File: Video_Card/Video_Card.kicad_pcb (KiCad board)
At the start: 4 copper layers, 159.8 x 100 mm, 9 parts, among them J1 DIN41612_03x32_ABC_COMETbus, U1 74FCT16245, U2 74FCT162244, U3 74FCT162244

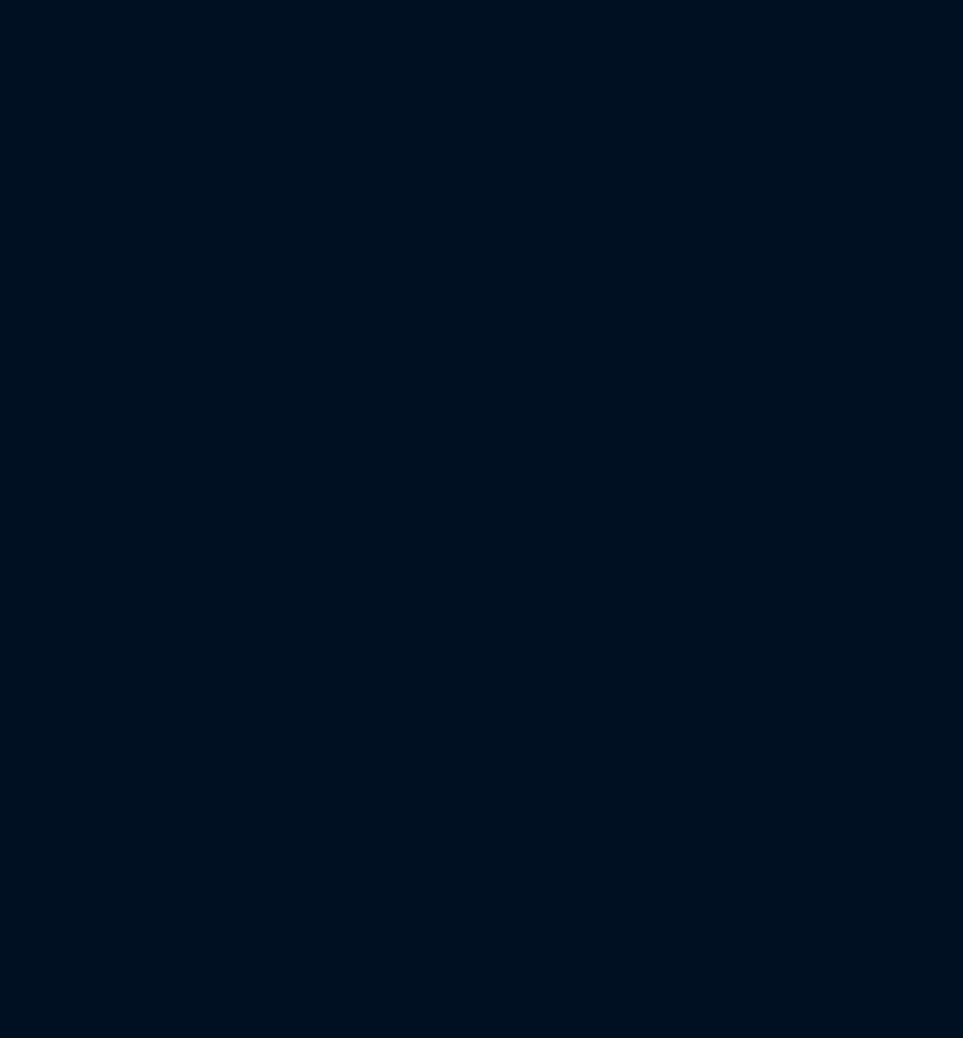
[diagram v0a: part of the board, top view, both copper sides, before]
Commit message: Todays work:
* Added clock identifier to SPI flash clock input
* Add config pins to FPGA host interface - can be used for configuring address decoding
* Add FPGA clocks sheet
* Add expansion ROM sheet
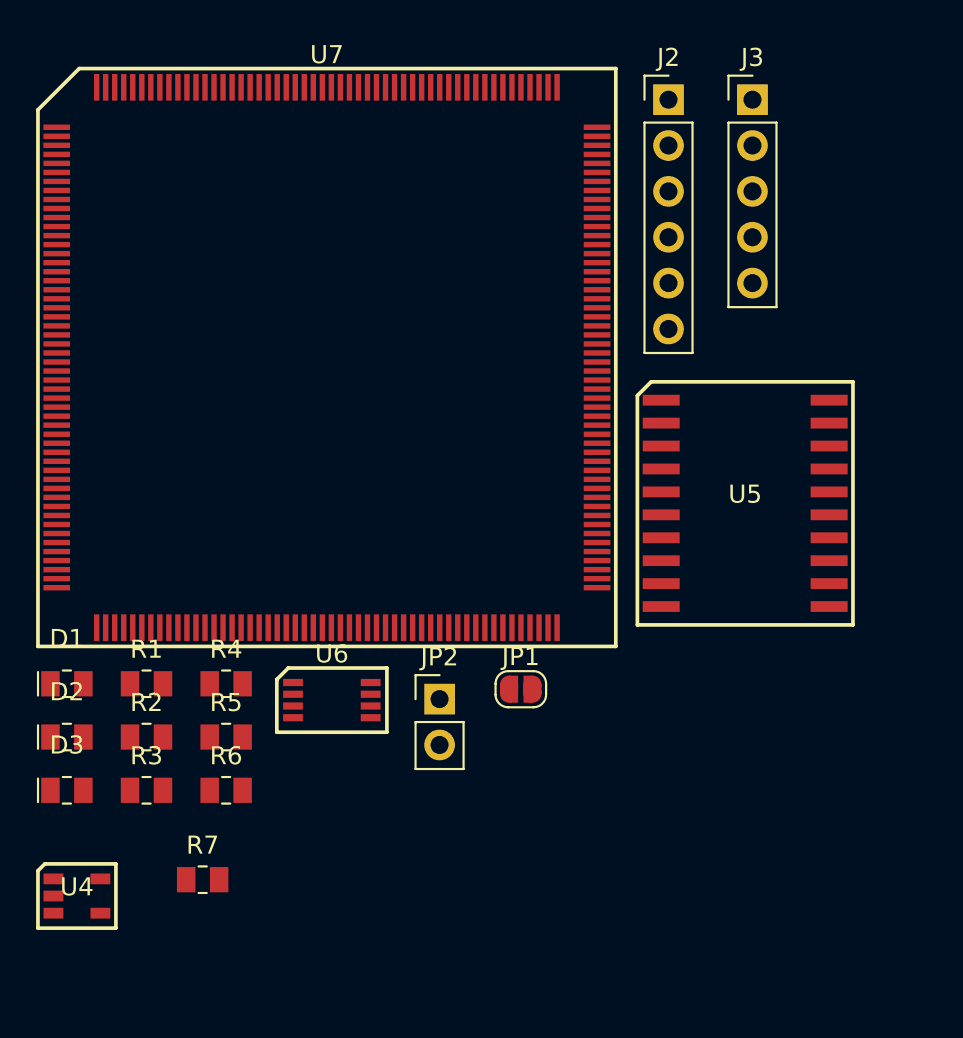
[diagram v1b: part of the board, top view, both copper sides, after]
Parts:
- added D1: GREEN, COMET_footprints:LED_SMD0805, F.Cu at (53.4, -24.1)
- added D2: GREEN, COMET_footprints:LED_SMD0805, F.Cu at (53.4, -21.2)
- added D3: RED, COMET_footprints:LED_SMD0805, F.Cu at (53.4, -18.2)
- added J2: Conn_01x06_Pin, Connector_PinHeader_2.54mm:PinHeader_1x06_P2.54mm_Vertical, F.Cu at (86.7, -56.5)
- added J3: Conn_01x05_Socket, Connector_PinHeader_2.54mm:PinHeader_1x05_P2.54mm_Vertical, F.Cu at (91.4, -56.5)
- added JP1: SolderJumper_2_Open, Jumper:SolderJumper-2_P1.3mm_Open_RoundedPad1.0x1.5mm, F.Cu at (78.5, -23.8)
- added JP2: Jumper_2_Open, Connector_PinHeader_2.54mm:PinHeader_1x02_P2.54mm_Vertical, F.Cu at (74.0, -23.3)
- added R1: 10K, COMET_footprints:R_SMD0805, F.Cu at (57.8, -24.1)
- added R2: 1K, COMET_footprints:R_SMD0805, F.Cu at (57.8, -21.2)
- added R3: 1K, COMET_footprints:R_SMD0805, F.Cu at (57.8, -18.2)
- added R4: 1K, COMET_footprints:R_SMD0805, F.Cu at (62.2, -24.1)
- added R5: 1K, COMET_footprints:R_SMD0805, F.Cu at (62.2, -21.2)
- added R6: 1K, COMET_footprints:R_SMD0805, F.Cu at (62.2, -18.2)
- added R7: 10K, COMET_footprints:R_SMD0805, F.Cu at (60.9, -13.3)
- added U4: SN74AHCT1G32DBV, COMET_footprints:Package_SOT23-5, F.Cu at (53.9, -12.4)
- added U5: PIC18F15Q40, COMET_footprints:Package_SO20W, F.Cu at (91.0, -34.1)
- added U6: ~, COMET_footprints:Package_TSSOP-8_3x3mm_P0.65mm, F.Cu at (68.1, -23.2)
- added U7: EPF81188AQC208-3, COMET_footprints:Package_PQFP-208_28x28mm_P0.5mm, F.Cu at (67.8, -42.2)
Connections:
- J1 pad b10: Net-(J1-Padb10) -> ~{AEIN}
- J1 pad b11: Net-(J1-Padb10) -> ~{AEOUT}
- J1 pad b15: unconnected-(J1-Padb15) -> CONFDONE
- U1 pad 10: unconnected-(U1C-GND-Pad10) -> GND
- U1 pad 15: unconnected-(U1C-GND-Pad15) -> GND
- U1 pad 18: unconnected-(U1C-VCC-Pad18) -> +5V
- U1 pad 21: unconnected-(U1C-GND-Pad21) -> GND
- U1 pad 28: unconnected-(U1C-GND-Pad28) -> GND
- U1 pad 31: unconnected-(U1C-VCC-Pad31) -> +5V
- U1 pad 34: unconnected-(U1C-GND-Pad34) -> GND
- U1 pad 39: unconnected-(U1C-GND-Pad39) -> GND
- U1 pad 4: unconnected-(U1C-GND-Pad4) -> GND
- U1 pad 42: unconnected-(U1C-VCC-Pad42) -> +5V
- U1 pad 45: unconnected-(U1C-GND-Pad45) -> GND
- U1 pad 7: unconnected-(U1C-VCC-Pad7) -> +5V
- U2 pad 10: unconnected-(U2E-GND-Pad10) -> GND
- U2 pad 11: unconnected-(U2B-2Y3-Pad11) -> A9
- U2 pad 12: unconnected-(U2B-2Y4-Pad12) -> A8
- U2 pad 13: unconnected-(U2C-3Y1-Pad13) -> A7
- U2 pad 14: unconnected-(U2C-3Y2-Pad14) -> A6
- U2 pad 15: unconnected-(U2E-GND-Pad15) -> GND
- U2 pad 16: unconnected-(U2C-3Y3-Pad16) -> A5
- U2 pad 17: unconnected-(U2C-3Y4-Pad17) -> A4
- U2 pad 18: unconnected-(U2E-VCC-Pad18) -> +5V
- U2 pad 19: unconnected-(U2D-4Y1-Pad19) -> A3
- U2 pad 2: unconnected-(U2A-1Y1-Pad2) -> A15
- U2 pad 20: unconnected-(U2D-4Y2-Pad20) -> A2
- U2 pad 21: unconnected-(U2E-GND-Pad21) -> GND
- U2 pad 22: unconnected-(U2D-4Y3-Pad22) -> A1
- U2 pad 26: unconnected-(U2D-4A4-Pad26) -> GND
- U2 pad 27: unconnected-(U2D-4A3-Pad27) -> SA1
- U2 pad 28: unconnected-(U2E-GND-Pad28) -> GND
- U2 pad 29: unconnected-(U2D-4A2-Pad29) -> SA2
- U2 pad 3: unconnected-(U2A-1Y2-Pad3) -> A14
- U2 pad 30: unconnected-(U2D-4A1-Pad30) -> SA3
- U2 pad 31: unconnected-(U2E-VCC-Pad31) -> +5V
- U2 pad 32: unconnected-(U2C-3A4-Pad32) -> SA4
- U2 pad 33: unconnected-(U2C-3A3-Pad33) -> SA5
- U2 pad 34: unconnected-(U2E-GND-Pad34) -> GND
- U2 pad 35: unconnected-(U2C-3A2-Pad35) -> SA6
- U2 pad 36: unconnected-(U2C-3A1-Pad36) -> SA7
- U2 pad 37: unconnected-(U2B-2A4-Pad37) -> SA8
- U2 pad 38: unconnected-(U2B-2A3-Pad38) -> SA9
- U2 pad 39: unconnected-(U2E-GND-Pad39) -> GND
- U2 pad 4: unconnected-(U2E-GND-Pad4) -> GND
- U2 pad 40: unconnected-(U2B-2A2-Pad40) -> SA10
- U2 pad 41: unconnected-(U2B-2A1-Pad41) -> SA11
- U2 pad 42: unconnected-(U2E-VCC-Pad42) -> +5V
- U2 pad 43: unconnected-(U2A-1A4-Pad43) -> SA12
- U2 pad 44: unconnected-(U2A-1A3-Pad44) -> SA13
- U2 pad 45: unconnected-(U2E-GND-Pad45) -> GND
- U2 pad 46: unconnected-(U2A-1A2-Pad46) -> SA14
- U2 pad 47: unconnected-(U2A-1A1-Pad47) -> SA15
- U2 pad 5: unconnected-(U2A-1Y3-Pad5) -> A13
- U2 pad 6: unconnected-(U2A-1Y4-Pad6) -> A12
- U2 pad 7: unconnected-(U2E-VCC-Pad7) -> +5V
- U2 pad 8: unconnected-(U2B-2Y1-Pad8) -> A11
- U2 pad 9: unconnected-(U2B-2Y2-Pad9) -> A10
- U3 pad 10: unconnected-(U3E-GND-Pad10) -> GND
- U3 pad 11: unconnected-(U3B-2Y3-Pad11) -> FC2
- U3 pad 12: unconnected-(U3B-2Y4-Pad12) -> ~{AS}
- U3 pad 13: unconnected-(U3C-3Y1-Pad13) -> A23
- U3 pad 14: unconnected-(U3C-3Y2-Pad14) -> A22
- U3 pad 15: unconnected-(U3E-GND-Pad15) -> GND
- U3 pad 16: unconnected-(U3C-3Y3-Pad16) -> A21
- U3 pad 17: unconnected-(U3C-3Y4-Pad17) -> A20
- U3 pad 18: unconnected-(U3E-VCC-Pad18) -> +5V
- U3 pad 19: unconnected-(U3D-4Y1-Pad19) -> A19
- U3 pad 2: unconnected-(U3A-1Y1-Pad2) -> ~{SYSRESET}
- U3 pad 20: unconnected-(U3D-4Y2-Pad20) -> A18
- U3 pad 21: unconnected-(U3E-GND-Pad21) -> GND
- U3 pad 22: unconnected-(U3D-4Y3-Pad22) -> A17
- U3 pad 23: unconnected-(U3D-4Y4-Pad23) -> A16
- U3 pad 26: unconnected-(U3D-4A4-Pad26) -> SA16
- U3 pad 27: unconnected-(U3D-4A3-Pad27) -> SA17
- U3 pad 28: unconnected-(U3E-GND-Pad28) -> GND
- U3 pad 29: unconnected-(U3D-4A2-Pad29) -> SA18
- U3 pad 3: unconnected-(U3A-1Y2-Pad3) -> ~{UDS}
- U3 pad 30: unconnected-(U3D-4A1-Pad30) -> SA19
- U3 pad 31: unconnected-(U3E-VCC-Pad31) -> +5V
- U3 pad 32: unconnected-(U3C-3A4-Pad32) -> SA20
- U3 pad 33: unconnected-(U3C-3A3-Pad33) -> SA21
- U3 pad 34: unconnected-(U3E-GND-Pad34) -> GND
- U3 pad 35: unconnected-(U3C-3A2-Pad35) -> SA22
- U3 pad 36: unconnected-(U3C-3A1-Pad36) -> SA23
- U3 pad 37: unconnected-(U3B-2A4-Pad37) -> ~{AS`}
- U3 pad 38: unconnected-(U3B-2A3-Pad38) -> FC2`
- U3 pad 39: unconnected-(U3E-GND-Pad39) -> GND
- U3 pad 4: unconnected-(U3E-GND-Pad4) -> GND
- U3 pad 40: unconnected-(U3B-2A2-Pad40) -> FC1`
- U3 pad 41: unconnected-(U3B-2A1-Pad41) -> FC0`
- U3 pad 42: unconnected-(U3E-VCC-Pad42) -> +5V
- U3 pad 43: unconnected-(U3A-1A4-Pad43) -> ~{WRITE`}
- U3 pad 44: unconnected-(U3A-1A3-Pad44) -> ~{LDS`}
- U3 pad 45: unconnected-(U3E-GND-Pad45) -> GND
- U3 pad 46: unconnected-(U3A-1A2-Pad46) -> ~{UDS`}
- U3 pad 47: unconnected-(U3A-1A1-Pad47) -> ~{SYSRESET`}
- U3 pad 5: unconnected-(U3A-1Y3-Pad5) -> ~{LDS}
- U3 pad 6: unconnected-(U3A-1Y4-Pad6) -> ~{WRITE}
- U3 pad 7: unconnected-(U3E-VCC-Pad7) -> +5V
- U3 pad 8: unconnected-(U3B-2Y1-Pad8) -> FC0
- U3 pad 9: unconnected-(U3B-2Y2-Pad9) -> FC1

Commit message: Work to date
So much to list ....

* Changed expansion ROM to 16 bit wide to remove some components
* Tried moving peripherals over to an 8 bit dedicated bus, but will have to revert this to reduce component count
* Fleshed out keyboard and I2C controller circuits
* Tried to fit in a font RAM, but I am 50/50 whether this will stick

And a lot more I am sure.
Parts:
- removed the D1 at (53.4, -24.1)
- added C1: 100nF, COMET_footprints:C_SMD0805, F.Cu at (87.1, 128.3)
- added C10: 100pF, COMET_footprints:C_SMD0805, F.Cu at (78.7, 127.3)
- added C2: 22uF, COMET_footprints:C_SMD_3.2MMx6.0MM, F.Cu at (85.6, 140.2)
- added C3: 100nF, COMET_footprints:C_SMD0805, F.Cu at (83.3, 134.6)
- added C4: 100nF, COMET_footprints:C_SMD0805, F.Cu at (99.8, 120.8)
- added C5: 47uF, COMET_footprints:C_SMD_3.2MMx6.0MM, F.Cu at (112.9, 138.8)
- added C6: 100nF, COMET_footprints:C_SMD0805, F.Cu at (5.44, 116.0)
- added C7: 100nF, COMET_footprints:C_SMD0805, F.Cu at (25.5, 133.9)
- added C8: 100nF, COMET_footprints:C_SMD0805, F.Cu at (77.7, 65.3)
- added C9: 100pF, COMET_footprints:C_SMD0805, F.Cu at (76.5, 127.3)
- added D4: 1N4148W, COMET_footprints:D_SOD-123, F.Cu at (99.7, 135.5)
- added D5: BAV99, COMET_footprints:Package_SOT-23, F.Cu at (82.7, 130.3)
- added D6: BAV99, COMET_footprints:Package_SOT-23, F.Cu at (83.5, 124.8)
- added D7: BAV99, COMET_footprints:Package_SOT-23, F.Cu at (87.2, 124.8)
- added D8: GREEN, COMET_footprints:LED_SMD0805, F.Cu at (128.8, 83.4)
- added F1: 2920L150DR, COMET_footprints:Fuse_2920_7451Metric, F.Cu at (76.5, 55.8)
- added HS1: ~, Video_Card:28MM-HEATSINK, F.Cu at (155.4, 79.6)
- added J4: DE15_Receptacle_HighDensity_MountingHoles, Video_Card:DSUB-15-HD_Female_Horizontal_P2.29x1.90mm_EdgePinOffset3.03mm_Housed_MountingHolesOffset4.94mm, F.Cu at (71.3, 124.2)
- added J5: Mini-DIN-6, Video_Card:Connector_MiniDIN-6, F.Cu at (64.0, 75.3)
- added J6: Mini-DIN-6, Video_Card:Connector_MiniDIN-6, F.Cu at (63.9, 92.8)
- added JP3: Jumper_2_Open, Connector_PinHeader_2.54mm:PinHeader_1x02_P2.54mm_Vertical, F.Cu at (36.4, 48.0)
- added JP4: Jumper_2_Open, Connector_PinHeader_2.54mm:PinHeader_1x02_P2.54mm_Vertical, F.Cu at (22.8, 65.5)
- added L1: ?, COMET_footprints:L_1812_4532Metric, F.Cu at (87.1, 133.1)
- added R10: 10K, COMET_footprints:R_SMD0805, F.Cu at (-3.38, 50.0)
- added R11: 10K, COMET_footprints:R_SMD0805, F.Cu at (31.9, 67.8)
- added R12: 0R, COMET_footprints:R_SMD0805, F.Cu at (-3.38, 53.0)
- added R13: 0R, COMET_footprints:R_SMD0805, F.Cu at (21.0, 84.4)
- added R14: 0R, COMET_footprints:R_SMD0805, F.Cu at (21.0, 87.3)
- added R15: 10K, COMET_footprints:R_SMD0805, F.Cu at (25.5, 136.8)
- added R16: 10K, COMET_footprints:R_SMD0805, F.Cu at (25.5, 139.8)
- added R17: 0R, COMET_footprints:R_SMD0805, F.Cu at (29.9, 133.9)
- added R18: 0R, COMET_footprints:R_SMD0805, F.Cu at (29.9, 136.8)
- added R19: 1K5, COMET_footprints:R_SMD0805, F.Cu at (-3.38, 55.9)
- added R20: 15R, COMET_footprints:R_MiniMELF_MMA-0204, F.Cu at (101.0, 131.4)
- added R21: 150R, COMET_footprints:R_MiniMELF_MMA-0204, F.Cu at (98.2, 131.4)
- added R22: 75R, COMET_footprints:R_MiniMELF_MMA-0204, F.Cu at (78.5, 141.7)
- added R23: 75R, COMET_footprints:R_MiniMELF_MMA-0204, F.Cu at (78.5, 138.9)
- added R24: 75R, COMET_footprints:R_MiniMELF_MMA-0204, F.Cu at (78.5, 136.1)
- added R25: 10K, COMET_footprints:R_SMD0805, F.Cu at (29.9, 139.8)
- added R26: 0R, COMET_footprints:R_SMD0805, F.Cu at (-16.0, 109.3)
- added R27: 10K, COMET_footprints:R_SMD0805, F.Cu at (-21.5, 134.3)
- added R28: 10K, COMET_footprints:R_SMD0805, F.Cu at (-21.5, 137.2)
- added R29: 10K, COMET_footprints:R_SMD0805, F.Cu at (5.44, 119.0)
- added R30: 10K, COMET_footprints:R_SMD0805, F.Cu at (5.44, 121.9)
- added R31: 1K5, COMET_footprints:R_SMD0805, F.Cu at (5.44, 124.9)
- added R32: 1K5, COMET_footprints:R_SMD0805, F.Cu at (5.44, 127.8)
- added R33: 1K5, COMET_footprints:R_SMD0805, F.Cu at (76.7, 122.3)
- added R34: 1K5, COMET_footprints:R_SMD0805, F.Cu at (79.7, 122.3)
- added R35: 1K5, COMET_footprints:R_SMD0805, F.Cu at (5.44, 136.7)
- added R36: 1K, COMET_footprints:R_SMD0805, F.Cu at (132.5, 83.4)
- added R37: 1K5, COMET_footprints:R_SMD0805, F.Cu at (34.4, 133.9)
- added R38: 0R, COMET_footprints:R_SMD0805, F.Cu at (34.4, 136.8)
- added R39: 0R, COMET_footprints:R_SMD0805, F.Cu at (34.4, 139.8)
- added R4: 1K, COMET_footprints:R_SMD0805, F.Cu at (67.7, 65.2)
- added R44: 10K, COMET_footprints:R_SMD0805, F.Cu at (112.3, 93.6)
- added R45: 10K, COMET_footprints:R_SMD0805, F.Cu at (112.3, 91.2)
- added R46: 1K5, COMET_footprints:R_SMD0805, F.Cu at (90.2, 70.4)
- added R47: 1K5, COMET_footprints:R_SMD0805, F.Cu at (92.7, 70.4)
- added R48: 1K5, COMET_footprints:R_SMD0805, F.Cu at (90.0, 95.6)
- added R49: 1K5, COMET_footprints:R_SMD0805, F.Cu at (92.6, 95.6)
- added R50: 470R, COMET_footprints:R_SMD0805, F.Cu at (73.4, 65.3)
- added R51: 33R, COMET_footprints:R_SMD0805, F.Cu at (76.5, 131.8)
- added R52: 33R, COMET_footprints:R_SMD0805, F.Cu at (78.7, 131.8)
- added R53: 10K, COMET_footprints:R_SMD0805, F.Cu at (25.5, 84.4)
- added R54: 10K, COMET_footprints:R_SMD0805, F.Cu at (25.5, 87.3)
- added R7: 1K, COMET_footprints:R_SMD0805, F.Cu at (31.9, 64.8)
- added R8: 10K, COMET_footprints:R_SMD0805, F.Cu at (-3.38, 44.1)
- added R9: 10K, COMET_footprints:R_SMD0805, F.Cu at (-3.38, 47.1)
- added RN2: 10K, Resistor_SMD:R_Cat16-4, F.Cu at (-28.3, 92.7)
- added RN3: 10K, Resistor_SMD:R_Cat16-4, F.Cu at (-24.4, 92.7)
- added RN4: 10K, Resistor_SMD:R_Cat16-4, F.Cu at (32.2, 99.8)
- added RN5: 10K, Resistor_SMD:R_Cat16-4, F.Cu at (36.1, 99.8)
- added RN6: 10K, Resistor_SMD:R_Cat16-4, F.Cu at (-17.4, 135.2)
- added SW1: SW_DIP_x06, Button_Switch_SMD:SW_DIP_SPSTx06_Slide_6.7x16.8mm_W8.61mm_P2.54mm_LowProfile, B.Cu at (132.8, 137.4)
- added TP1: TestPoint, TestPoint:TestPoint_Pad_D1.0mm, F.Cu at (21.8, 133.9)
- added TP2: TestPoint, TestPoint:TestPoint_Pad_D1.0mm, F.Cu at (21.8, 137.0)
- added TP3: TestPoint, TestPoint:TestPoint_Pad_D1.0mm, F.Cu at (21.8, 140.0)
- added U10: SN74AHCT1G125DBV, COMET_footprints:Package_SOT23-5, F.Cu at (-2.82, 75.2)
- added U11: M29F400FB55N3F2, COMET_footprints:Package_TSOP-I-48_18.4x12mm_P0.5mm, F.Cu at (120.1, 119.1)
- added U14: IMSG171-35, COMET_footprints:Package_DIP-28_W15.24mm_LongPads, F.Cu at (99.8, 124.2)
- added U15: LM334M/NOPB, COMET_footprints:Package_SO8, F.Cu at (99.8, 114.8)
- added U16: SN74CBT16212CDLR, COMET_footprints:Package_SSOP56-1, F.Cu at (158.4, 110.7)
- added U17: SN74CBT16212CDLR, COMET_footprints:Package_SSOP56-1, F.Cu at (172.0, 110.8)
- added U18: SN74CBT16212CDLR, COMET_footprints:Package_SSOP56-1, F.Cu at (185.4, 110.6)
- added U19: IS61C6416AL-12TLI, COMET_footprints:Package_TSOP-II-44_10.16x18.41mm_P0.8mm, F.Cu at (158.2, 133.6)
- added U20: IS61C6416AL-12TLI, COMET_footprints:Package_TSOP-II-44_10.16x18.41mm_P0.8mm, F.Cu at (172.9, 133.6)
- added U21: SN74LVC1G19DBV, COMET_footprints:Package_SOT23-6, F.Cu at (-20.9, 110.2)
- added U22: IS61C6416AL-12TLI, COMET_footprints:Package_TSOP-II-44_10.16x18.41mm_P0.8mm, F.Cu at (187.6, 133.6)
- added U23: SST39SF010A-70-4C-NHE, COMET_footprints:Package_PLCC-32_SMD_socket, F.Cu at (138.9, 119.0)
- added U24: PCF8584T, COMET_footprints:Package_SO20W, F.Cu at (82.3, 112.0)
- added U25: VT82C42, COMET_footprints:Package_DIP-40_W15.24mm_LongPads, F.Cu at (91.4, 77.6)
- added U30: SN74AHCT1G32DBV, COMET_footprints:Package_SOT23-5, F.Cu at (23.7, 127.9)
- added U31: SN75452B, COMET_footprints:Package_DIP-8_W7.62mm_LongPads, F.Cu at (91.3, 62.5)
- added U32: SN75452B, COMET_footprints:Package_DIP-8_W7.62mm_LongPads, F.Cu at (91.4, 87.9)
- added U8: SN74LVC1G06DBV, COMET_footprints:Package_SOT23-5, F.Cu at (-2.82, 65.7)
- added U9: SN74LVC1G06DBV, COMET_footprints:Package_SOT23-5, F.Cu at (-2.82, 70.4)
- added Y1: 40MHz, COMET_footprints:Oscillator_SMD_XO91-4Pin_7.0x5.0mm, F.Cu at (182.6, 81.5)
- added Y2: 28.322MHz, COMET_footprints:Oscillator_DIP-8-14, F.Cu at (112.5, 58.5)
- added Y3: 25.175MHz, COMET_footprints:Oscillator_DIP-8-14, F.Cu at (112.8, 72.3)
- D1: value IN_USE -> GREEN
- R2, R3: value 1K -> 1K5
- U5: value PIC18F15Q40 -> PIC18F15Q40-I/SS; footprint COMET_footprints:Package_SO20W -> Video_Card:Package_SSOP-20_5.3x7.2mm_P0.65_MCHP
- U6: value ~ -> M95M04-DRDW6; footprint COMET_footprints:Package_TSSOP-8_3x3mm_P0.65mm -> COMET_footprints:Package_TSSOP-8_4.4x3mm_P0.65mm
- moved U7 150.1 mm to (155.4, 79.6), turned to 90 degrees
- moved D3 131.1 mm to (163.2, 53.3), turned to -90 degrees
- moved D2 130.8 mm to (160.9, 53.3), turned to -90 degrees
- moved R6 126.1 mm to (163.2, 57.3), turned to 90 degrees
- moved R5 126.1 mm to (160.9, 57.3), turned to 90 degrees
- moved J3 120.0 mm to (126.5, 58.3), turned to 90 degrees
- moved U6 118.6 mm to (156.8, 55.4), turned to 90 degrees
- moved J2 117.1 mm to (126.5, 53.7), turned to 90 degrees
- moved U5 106.4 mm to (148.5, 55.4), turned to 90 degrees
- moved JP1 38.2 mm to (71.9, 13.8)
- moved JP2 38.2 mm to (67.4, 14.4)
- moved R1 38.2 mm to (51.2, 13.5)
- moved R2 38.2 mm to (51.2, 16.5)
- moved R3 38.2 mm to (51.2, 19.4)
- moved R4 38.2 mm to (55.6, 13.5)
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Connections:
- D2 pad 1: Net-(D2-K) -> GND
- D3 pad 1: Net-(D3-K) -> GND
- J1 pad b10: ~{AEIN} -> Net-(J1B-~{AEIN})
- J1 pad b11: ~{AEOUT} -> Net-(J1B-~{AEIN})
- J1 pad b15: CONFDONE -> unconnected-(J1B-CONFDONE-Padb15)
- J3 pad 1: ~{SYSRESET} -> Net-(J3-Pin_1)
- R5 pad 1: Net-(D2-A) -> Net-(U5-LED_RUN)
- R5 pad 2: +5V -> Net-(D2-A)
- R6 pad 1: Net-(D3-A) -> Net-(U5-LED_FAIL)
- R6 pad 2: +5V -> Net-(D3-A)
- U5 pad 16: Net-(D3-K) -> Net-(U5-LED_FAIL)
- U5 pad 17: Net-(D2-K) -> Net-(U5-LED_RUN)
- U5 pad 4: ~{SYSRESET} -> Net-(J3-Pin_1)
- U5 pad 5: (no net) -> ~{FPGA_RESET}
- U7 pad 10: (no net) -> Net-(U14A-~{WR})
- U7 pad 100: (no net) -> A14
- U7 pad 101: (no net) -> A15
- U7 pad 112: (no net) -> DDIR
- U7 pad 116: (no net) -> SYSCLK
- U7 pad 117: (no net) -> D7
- U7 pad 118: (no net) -> D4
- U7 pad 120: (no net) -> D15
- U7 pad 121: (no net) -> D0
- U7 pad 125: (no net) -> A17
- U7 pad 126: (no net) -> Net-(RN2-R2.1)
- U7 pad 127: (no net) -> A19
- U7 pad 128: (no net) -> A20
- U7 pad 129: (no net) -> FC2
- U7 pad 13: (no net) -> ~{WRITE}
- U7 pad 130: (no net) -> FC0
- U7 pad 133: (no net) -> ~{UDS}
- U7 pad 134: (no net) -> A11
- U7 pad 135: (no net) -> ~{LDS}
- U7 pad 136: (no net) -> A2
- U7 pad 137: (no net) -> D13
- U7 pad 14: (no net) -> D3
- U7 pad 141: (no net) -> Net-(U14A-PCLK)
- U7 pad 142: (no net) -> D9
- U7 pad 144: (no net) -> D12
- U7 pad 145: (no net) -> D2
- U7 pad 146: (no net) -> ~{FPGA_RESET}
- U7 pad 149: (no net) -> Net-(U14A-P2)
- U7 pad 15: (no net) -> D1
- U7 pad 153: (no net) -> Net-(U14A-P3)
- U7 pad 160: (no net) -> A16
- U7 pad 162: (no net) -> A21
- U7 pad 163: (no net) -> A22
- U7 pad 164: (no net) -> A13
- U7 pad 167: (no net) -> Net-(U7F-VSYNC)
- U7 pad 169: (no net) -> Net-(U7F-CLK_25)
- U7 pad 17: (no net) -> D11
- U7 pad 170: (no net) -> Net-(U7F-HSYNC)
- U7 pad 173: (no net) -> Net-(U14A-P6)
- U7 pad 179: (no net) -> ~{DBEN}
- U7 pad 180: (no net) -> Net-(U7C-BERR_DRV)
- U7 pad 202: (no net) -> Net-(U7F-VID_ACT)
- U7 pad 22: (no net) -> A4
- U7 pad 23: (no net) -> A3
- U7 pad 24: (no net) -> D14
- U7 pad 25: (no net) -> D10
- U7 pad 26: (no net) -> A12
- U7 pad 29: (no net) -> FC1
- U7 pad 30: (no net) -> ~{AS}
- U7 pad 31: (no net) -> A18
- U7 pad 32: (no net) -> Net-(RN2-R1.1)
- U7 pad 37: (no net) -> D8
- U7 pad 38: (no net) -> D6
- U7 pad 39: (no net) -> D5
- U7 pad 40: (no net) -> Net-(U14A-P1)
- U7 pad 41: (no net) -> A1
- U7 pad 66: (no net) -> Net-(U14A-P0)
- U7 pad 7: (no net) -> Net-(U14A-P4)
- U7 pad 8: (no net) -> Net-(U14A-~{RD})
- U7 pad 83: (no net) -> Net-(U14A-~{BLANK})
- U7 pad 86: (no net) -> Net-(U14A-P7)
- U7 pad 90: (no net) -> Net-(U14A-P5)
- U7 pad 92: (no net) -> Net-(U7C-DTACK_DRV)
- U7 pad 95: (no net) -> Net-(U7F-CLK_28)
- U7 pad 99: (no net) -> A23
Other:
- board text added: "KEYBOARD"
- board text added: "MOUSE"
- board text added: "VGA COMPATIBLE VIDEO CARD TOM STOREY JUN 2025 REV ${REVISION}"
- board text removed: "VGA COMPATIBLE VIDEO CARD TOM STOREY MAR 2025 REV ${REVISION}"

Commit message: Final tweaks before ordering
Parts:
- removed JP4: Jumper_2_Open, Connector_PinHeader_2.54mm:PinHeader_1x02_P2.54mm_Vertical
- removed the R4 at (67.7, 65.2)
- removed the R4 at (55.6, 13.5)
- removed the R7 at (31.9, 64.8)
- removed the R7 at (54.3, 24.4)
- removed REF** (x2): MountingHole_3.2mm_M3, MountingHole:MountingHole_3.2mm_M3
- removed U30: SN74AHCT1G32DBV, COMET_footprints:Package_SOT23-5
- removed U31, U32: SN75452B, COMET_footprints:Package_DIP-8_W7.62mm_LongPads
- added C11: 47uF, COMET_footprints:C_SMD_3.2MMx6.0MM, F.Cu at (106.0, 85.1)
- added C12: 100nF, COMET_footprints:C_SMD0805, B.Cu at (206.1, 103.5)
- added C13: 100nF, COMET_footprints:C_SMD0805, B.Cu at (206.1, 94.6)
- added C14: 100nF, COMET_footprints:C_SMD0805, B.Cu at (201.6, 120.7)
- added C15: 100nF, COMET_footprints:C_SMD0805, B.Cu at (201.6, 129.5)
- added C16: 100nF, COMET_footprints:C_SMD0805, B.Cu at (206.1, 129.5)
- added C17: 100nF, COMET_footprints:C_SMD0805, B.Cu at (206.1, 120.7)
- added C18: 100nF, COMET_footprints:C_SMD0805, B.Cu at (204.2, 80.0)
- added C19: 100nF, COMET_footprints:C_SMD0805, B.Cu at (204.2, 85.3)
- added C20: 100nF, COMET_footprints:C_SMD0805, B.Cu at (162.9, 56.5)
- added C21: 100nF, COMET_footprints:C_SMD0805, B.Cu at (152.7, 56.6)
- added C22: 100nF, COMET_footprints:C_SMD0805, F.Cu at (136.8, 72.2)
- added C23: 100nF, COMET_footprints:C_SMD0805, F.Cu at (136.8, 80.2)
- added C24: 100nF, COMET_footprints:C_SMD0805, F.Cu at (136.8, 87.8)
- added C25: 100nF, COMET_footprints:C_SMD0805, F.Cu at (136.8, 92.8)
- added C26: 100nF, COMET_footprints:C_SMD0805, F.Cu at (150.0, 103.0)
- added C27: 100nF, COMET_footprints:C_SMD0805, F.Cu at (158.0, 103.0)
- added C28: 100nF, COMET_footprints:C_SMD0805, F.Cu at (170.0, 103.0)
- added C29: 100nF, COMET_footprints:C_SMD0805, F.Cu at (176.8, 93.8)
- added C30: 100nF, COMET_footprints:C_SMD0805, F.Cu at (176.8, 87.8)
- added C31: 100nF, COMET_footprints:C_SMD0805, F.Cu at (176.8, 79.8)
- added C32: 100nF, COMET_footprints:C_SMD0805, F.Cu at (176.8, 73.8)
- added C33: 100nF, COMET_footprints:C_SMD0805, B.Cu at (165.5, 63.0)
- added C34: 100nF, COMET_footprints:C_SMD0805, B.Cu at (155.5, 63.0)
- added C35: 100nF, COMET_footprints:C_SMD0805, B.Cu at (148.5, 63.0)
- added C36: 100nF, COMET_footprints:C_SMD0805, B.Cu at (144.0, 114.0)
- added C37: 100nF, COMET_footprints:C_SMD0805, B.Cu at (165.2, 116.0)
- added C38: 100nF, COMET_footprints:C_SMD0805, B.Cu at (184.9, 116.0)
- added C39: 100nF, COMET_footprints:C_SMD0805, B.Cu at (155.6, 135.0)
- added C40: 100nF, COMET_footprints:C_SMD0805, B.Cu at (155.6, 140.2)
- added C41: 100nF, COMET_footprints:C_SMD0805, B.Cu at (110.5, 58.4)
- added C42: 100nF, COMET_footprints:C_SMD0805, B.Cu at (110.5, 71.8)
- added C43: 100nF, COMET_footprints:C_SMD0805, B.Cu at (177.4, 135.0)
- added C44: 100nF, COMET_footprints:C_SMD0805, B.Cu at (177.4, 140.2)
- added C45: 100nF, COMET_footprints:C_SMD0805, B.Cu at (125.1, 112.4)
- added C46: 100nF, COMET_footprints:C_SMD0805, B.Cu at (125.1, 120.7)
- added C47: 100nF, COMET_footprints:C_SMD0805, B.Cu at (125.1, 128.9)
- added C48: 100nF, COMET_footprints:C_SMD0805, B.Cu at (116.8, 116.2)
- added C49: 100nF, COMET_footprints:C_SMD0805, B.Cu at (186.2, 79.5)
- added C50: 100nF, COMET_footprints:C_SMD0805, B.Cu at (83.6, 116.8)
- added C51: 100nF, COMET_footprints:C_SMD0805, B.Cu at (88.5, 101.6)
- added C52: 100nF, COMET_footprints:C_SMD0805, B.Cu at (92.7, 88.9)
- added C53: 100nF, COMET_footprints:C_SMD0805, B.Cu at (92.7, 71.1)
- added C54: 100nF, COMET_footprints:C_SMD0805, B.Cu at (185.8, 101.0)
- added C55: 100nF, COMET_footprints:C_SMD0805, B.Cu at (106.7, 133.3)
- added C56: 47uF, COMET_footprints:C_SMD_3.2MMx6.0MM, F.Cu at (88.3, 136.7)
- added C57: 100pF, COMET_footprints:C_SMD0805, F.Cu at (75.6, 125.1)
- added C58: 100pF, COMET_footprints:C_SMD0805, F.Cu at (75.6, 120.7)
- added C59: 100nF, COMET_footprints:C_SMD0805, F.Cu at (79.4, 139.1)
- added C60: 22uF, COMET_footprints:C_SMD_3.2MMx6.0MM, F.Cu at (88.3, 141.6)
- added C61: 100nF, COMET_footprints:C_SMD0805, B.Cu at (98.8, 141.0)
- added C62: 100nF, COMET_footprints:C_SMD0805, F.Cu at (77.5, 56.8)
- added H1: MountingHole_3.2mm_M3, MountingHole:MountingHole_3.2mm_M3, F.Cu at (67.0, 53.5)
- added H2: MountingHole_3.2mm_M3, MountingHole:MountingHole_3.2mm_M3, F.Cu at (67.0, 142.1)
- added R4: 1K5, COMET_footprints:R_SMD0805, F.Cu at (168.6, 60.3)
- added R40: 0R, COMET_footprints:R_SMD0805, B.Cu at (121.9, 58.4)
- added R41: 15R, COMET_footprints:R_SMD0805, F.Cu at (91.4, 122.6)
- added R42: 150R, COMET_footprints:R_SMD0805, F.Cu at (89.2, 129.2)
- added R43: 0R, COMET_footprints:R_SMD0805, B.Cu at (121.9, 71.8)
- added R55: 10K, COMET_footprints:R_SMD0805, F.Cu at (76.2, 107.3)
- added R56: 1K5, COMET_footprints:R_SMD0805, F.Cu at (81.0, 95.7)
- added R57: 1K5, COMET_footprints:R_SMD0805, F.Cu at (81.0, 93.7)
- added R58: 1K5, COMET_footprints:R_SMD0805, F.Cu at (81.0, 75.9)
- added R59: 1K5, COMET_footprints:R_SMD0805, F.Cu at (81.0, 74.0)
- added R60: 10K, COMET_footprints:R_SMD0805, F.Cu at (104.8, 94.0)
- added R61: 10K, COMET_footprints:R_SMD0805, F.Cu at (104.8, 91.4)
- added R62: 0R, COMET_footprints:R_SMD0805, F.Cu at (104.8, 96.5)
- added R63: 10K, COMET_footprints:R_SMD0805, F.Cu at (104.8, 101.4)
- added R64: 10K, COMET_footprints:R_SMD0805, F.Cu at (104.8, 99.1)
- added R65: 470R, COMET_footprints:R_SMD0805, F.Cu at (77.5, 58.5)
- added R66: 10K, COMET_footprints:R_SMD0805, B.Cu at (113.3, 100.7)
- added R67: 0R, COMET_footprints:R_SMD0805, B.Cu at (73.4, 82.5)
- added R68: 0R, COMET_footprints:R_SMD0805, B.Cu at (75.3, 82.5)
- added R7: 1K, COMET_footprints:R_SMD0805, F.Cu at (168.6, 56.5)
- added RN10: 10K, COMET_footprints:R_Cat16-4, B.Cu at (160.1, 119.6)
- added RN11: 10K, COMET_footprints:R_Cat16-4, B.Cu at (151.8, 119.8)
- added RN12: 10K, COMET_footprints:R_Cat16-4, B.Cu at (140.8, 119.8)
- added RN13: 10K, COMET_footprints:R_Cat16-4, B.Cu at (146.3, 119.8)
- added RN7: 560R, COMET_footprints:R_Cat16-4, B.Cu at (134.5, 110.5)
- added RN8: 560R, COMET_footprints:R_Cat16-4, B.Cu at (134.5, 114.3)
- added RN9: 560R, COMET_footprints:R_Cat16-4, B.Cu at (134.5, 118.7)
- added TP4: TestPoint, TestPoint:TestPoint_Pad_D1.0mm, B.Cu at (141.2, 84.2)
- added TP5: TestPoint, TestPoint:TestPoint_Pad_D1.0mm, B.Cu at (145.2, 98.2)
- added TP6: TestPoint, TestPoint:TestPoint_Pad_D1.0mm, B.Cu at (154.2, 67.8)
- added U12: SN74CBT16212CDLR, COMET_footprints:Package_SSOP56-1, F.Cu at (165.7, 118.7)
- added U13: SN74CBT16212CDLR, COMET_footprints:Package_SSOP56-1, F.Cu at (185.4, 118.7)
- added U26: M95M04-DRDW6, COMET_footprints:Package_TSSOP-8_4.4x3mm_P0.65mm, F.Cu at (153.7, 56.5)
- added U27: PIC18F15Q40-I/SS, Video_Card:Package_SSOP-20_5.3x7.2mm_P0.65_MCHP, F.Cu at (160.0, 56.5)
- added U28: IMSG171-35, Video_Card:Package_DIP-28_W15.24mm_3x7mil, F.Cu at (102.9, 124.5)
- added U29: LM334M/NOPB, COMET_footprints:Package_SO8, F.Cu at (85.7, 121.9)
- C1, C3, C4, C6, R11, R12, R13, R14, R15, R18, R25, R27, R28, R5, TP1, TP2, TP3: moved to B.Cu
- C10, C9: value 100pF -> 47uF; footprint COMET_footprints:C_SMD0805 -> COMET_footprints:C_SMD_3.2MMx6.0MM
- C2: value 22uF -> 100nF; footprint COMET_footprints:C_SMD_3.2MMx6.0MM -> COMET_footprints:C_SMD0805; moved to B.Cu
- C5: value 47uF -> 100nF; footprint COMET_footprints:C_SMD_3.2MMx6.0MM -> COMET_footprints:C_SMD0805; moved to B.Cu
- C7, C8: value 100nF -> 100uF; footprint COMET_footprints:C_SMD0805 -> COMET_footprints:C_SMD_4.3MMx7.3MM
- D5: value BAV99 -> GREEN; footprint COMET_footprints:Package_SOT-23 -> COMET_footprints:LED_SMD0805
- D8: value GREEN -> BAV99; footprint COMET_footprints:LED_SMD0805 -> COMET_footprints:Package_SOT-23
- F1: value 2920L150DR -> 1210L200PR; footprint COMET_footprints:Fuse_2920_7451Metric -> COMET_footprints:Fuse_1210_3225Metric
- JP1: value SolderJumper_2_Open -> Jumper_2_Open; footprint Jumper:SolderJumper-2_P1.3mm_Open_RoundedPad1.0x1.5mm -> Connector_PinHeader_2.54mm:PinHeader_1x02_P2.54mm_Vertical
- JP2: value Jumper_2_Open -> SolderJumper_2_Open; footprint Connector_PinHeader_2.54mm:PinHeader_1x02_P2.54mm_Vertical -> Jumper:SolderJumper-2_P1.3mm_Open_TrianglePad1.0x1.5mm; moved to B.Cu
- R10: value 10K -> 0R
- R16, R29, R30: value 10K -> 0R; moved to B.Cu
- R17, R26: value 0R -> 10K; moved to B.Cu
- R19, R33, R34, R35: value 1K5 -> 10K; moved to B.Cu
- R2: value 1K5 -> 10K
- R20: value 15R -> 10K; footprint COMET_footprints:R_MiniMELF_MMA-0204 -> COMET_footprints:R_SMD0805; moved to B.Cu
- R21: value 150R -> 10K; footprint COMET_footprints:R_MiniMELF_MMA-0204 -> COMET_footprints:R_SMD0805; moved to B.Cu
- R22, R23, R24: value 75R -> 10K; footprint COMET_footprints:R_MiniMELF_MMA-0204 -> COMET_footprints:R_SMD0805; moved to B.Cu
- R31, R32: value 1K5 -> 0R; moved to B.Cu
- R36: value 1K -> 1K5; moved to B.Cu
- R37: value 1K5 -> 150R
- R38, R39: value 0R -> 150R
- R46, R47: value 1K5 -> 33R
- R48: value 1K5 -> 1K
- R50: value 470R -> 1K5
- R51: value 33R -> 1K5
- R52: value 33R -> 10K
- R53, R54, R9: value 10K -> 1K5
- R8: value 10K -> 1K
- RN2, RN3, RN4, RN5, RN6: footprint Resistor_SMD:R_Cat16-4 -> COMET_footprints:R_Cat16-4; moved to B.Cu
- SW1: footprint Button_Switch_SMD:SW_DIP_SPSTx06_Slide_6.7x16.8mm_W8.61mm_P2.54mm_LowProfile -> Video_Card:SW_DIP_SPSTx06_Slide_6.7x16.8mm_W6.73mm_P2.54mm_LowProfile_JPin; moved to F.Cu
- U10: value SN74AHCT1G125DBV -> SN74LVC1G06DBV
- U11: value M29F400FB55N3F2 -> SN74CBT16212CDLR; footprint COMET_footprints:Package_TSOP-I-48_18.4x12mm_P0.5mm -> COMET_footprints:Package_SSOP56-1
- U14: value IMSG171-35 -> IS61C6416AL-12TLI; footprint COMET_footprints:Package_DIP-28_W15.24mm_LongPads -> COMET_footprints:Package_TSOP-II-44_10.16x18.41mm_P0.8mm
- U15: value LM334M/NOPB -> IS61C6416AL-12TLI; footprint COMET_footprints:Package_SO8 -> COMET_footprints:Package_TSOP-II-44_10.16x18.41mm_P0.8mm
- U16: value SN74CBT16212CDLR -> IS62C256AL-45TLI; footprint COMET_footprints:Package_SSOP56-1 -> Video_Card:Package_TSOP-I-28_11.8x8mm_P0.55mm
- U17, U18: value SN74CBT16212CDLR -> CY74FCT245TQCT; footprint COMET_footprints:Package_SSOP56-1 -> COMET_footprints:Package_QSOP20
- U19: value IS61C6416AL-12TLI -> CY74FCT245TQCT; footprint COMET_footprints:Package_TSOP-II-44_10.16x18.41mm_P0.8mm -> COMET_footprints:Package_QSOP20
- U20: value IS61C6416AL-12TLI -> M29F400FB55N3F2; footprint COMET_footprints:Package_TSOP-II-44_10.16x18.41mm_P0.8mm -> Video_Card:Package_TSOP-I-48_18.4x12mm_P0.5mm
- U21: value SN74LVC1G19DBV -> PCF8584T; footprint COMET_footprints:Package_SOT23-6 -> COMET_footprints:Package_SO20W
- U22: value IS61C6416AL-12TLI -> VT82C42; footprint COMET_footprints:Package_TSOP-II-44_10.16x18.41mm_P0.8mm -> Video_Card:Package_DIP-40_W15.24mm_3x7mil
- U23: value SST39SF010A-70-4C-NHE -> SN74AHCT1G32DBV; footprint COMET_footprints:Package_PLCC-32_SMD_socket -> COMET_footprints:Package_SOT23-5
- U24: value PCF8584T -> SN75452B; footprint COMET_footprints:Package_SO20W -> Video_Card:Package_DIP-8_W7.62mm_3x7mil
- U25: value VT82C42 -> SN75452B; footprint COMET_footprints:Package_DIP-40_W15.24mm_LongPads -> Video_Card:Package_DIP-8_W7.62mm_3x7mil
- U5: value PIC18F15Q40-I/SS -> EPF81188AQC208-3; footprint Video_Card:Package_SSOP-20_5.3x7.2mm_P0.65_MCHP -> COMET_footprints:Package_PQFP-208_28x28mm_P0.5mm
- U6: value M95M04-DRDW6 -> SN74LVC1G06DBV; footprint COMET_footprints:Package_TSSOP-8_4.4x3mm_P0.65mm -> COMET_footprints:Package_SOT23-5
- U7: value EPF81188AQC208-3 -> SN74LVC1G06DBV; footprint COMET_footprints:Package_PQFP-208_28x28mm_P0.5mm -> COMET_footprints:Package_SOT23-5
- U8: value SN74LVC1G06DBV -> SN74AHCT1G125DBV
- Y1: footprint COMET_footprints:Oscillator_SMD_XO91-4Pin_7.0x5.0mm -> COMET_footprints:Oscillator_SMD_7.0x5.0mm
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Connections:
- C10 pad 1: Net-(C10-Pad1) -> +5V
- C2 pad 1: VAA -> +5V
- C3 pad 1: VAA -> +5V
- C4 pad 1: VAA -> +5V
- C4 pad 2: Net-(U14A-IREF) -> GND
- C5 pad 1: VAA -> +5V
- C5 pad 2: Net-(U14A-IREF) -> GND
- C8 pad 1: +5VP -> +5V
- C9 pad 1: Net-(C9-Pad1) -> +5V
- D4 pad 2: Net-(D4-A) -> /RAMDAC/SINK
- D5 pad 1: GND -> Net-(D5-K)
- D5 pad 2: VAA -> Net-(D5-A)
- D6 pad 3: /RAMDAC/G -> /RAMDAC/R
- D7 pad 3: /RAMDAC/B -> /RAMDAC/G
- D8 pad 2: Net-(D8-A) -> VAA
- J1 pad b29: unconnected-(J1B-~{IRQ2}-Padb29) -> IRQ2
- J4 pad 0: Net-(JP4-B) -> GND
- J4 pad 13: Net-(C9-Pad1) -> Net-(C57-Pad1)
- J4 pad 14: Net-(C10-Pad1) -> Net-(C58-Pad1)
- J5 pad 0: (no net) -> GND
- J5 pad 1: Net-(U25A-P10) -> Net-(U22A-P10)
- J5 pad 2: unconnected-(J5-Pad2) -> Net-(J5-Pad2)
- J5 pad 5: Net-(U25A-T0) -> Net-(U22A-T0)
- J5 pad 6: unconnected-(J5-Pad6) -> Net-(J5-Pad6)
- J6 pad 0: (no net) -> GND
- J6 pad 1: Net-(U25A-P11) -> Net-(U22A-P11)
- J6 pad 5: Net-(U25A-T1) -> Net-(U22A-T1)
- JP1 pad 1: Net-(J2-Pin_3) -> Net-(JP1-A)
- JP1 pad 2: +5V -> Net-(J3-Pin_1)
- JP2 pad 1: Net-(JP2-A) -> Net-(J2-Pin_3)
- JP2 pad 2: GND -> +5V
- JP3 pad 2: Net-(J3-Pin_1) -> GND
- R1 pad 2: Net-(U5-~{SS}) -> Net-(U26-~{SS})
- R10 pad 1: ~{DBEN} -> Net-(Y1-OUT)
- R10 pad 2: +5V -> Net-(U5C-CLK_40)
- R11 pad 1: +5V -> ~{IACKIN}
- R11 pad 2: Net-(J3-Pin_1) -> +5V
- R12 pad 1: Net-(Y1-OUT) -> Net-(R12-Pad1)
- R12 pad 2: Net-(U7C-CLK_40) -> ~{IRQ6}
- R13 pad 1: Net-(Y2-OUT) -> Net-(R12-Pad1)
- R13 pad 2: Net-(U7F-CLK_28) -> ~{IRQ5}
- R14 pad 1: Net-(Y3-OUT) -> Net-(R12-Pad1)
- R14 pad 2: Net-(U7F-CLK_25) -> ~{IRQ4}
- R15 pad 1: +5V -> ~{DBEN}
- R15 pad 2: Net-(U11A-~{BYTE}) -> +5V
- R16 pad 1: +5V -> Net-(R16-Pad1)
- R16 pad 2: Net-(U11A-~{RST}) -> ~{IRQ3}
- R17 pad 1: A15 -> GND
- R17 pad 2: Net-(U11A-A14) -> /FPGA host interface/DTACK_DRV
- R18 pad 1: GND -> Net-(R16-Pad1)
- R18 pad 2: Net-(U11A-A14) -> IRQ2
- R19 pad 1: ~{FPGA_RESET} -> GND
- R19 pad 2: +5V -> /FPGA host interface/BERR_DRV
- R2 pad 2: Net-(U5-CONF_DONE) -> Net-(J3-Pin_1)
- R20 pad 1: Net-(D4-A) -> GND
- R20 pad 2: Net-(R20-Pad2) -> /FPGA host interface/IRQ_HI_DRV
- R21 pad 1: Net-(R20-Pad2) -> GND
- R21 pad 2: GND -> /FPGA host interface/IRQ_LO_DRV
- R22 pad 1: /RAMDAC/R -> +5V
- R22 pad 2: GND -> ~{REGEN_CS}
- R23 pad 1: /RAMDAC/G -> +5V
- R23 pad 2: GND -> ~{BANK_CS}
- R24 pad 1: /RAMDAC/B -> FONTSEL
- R25 pad 1: +5V -> Net-(U16A-~{CE})
- R25 pad 2: Net-(U11A-~{CE}) -> GND
- R26 pad 1: ~{B0CS} -> Net-(U16A-~{OE})
- R26 pad 2: Net-(U19A-~{CE}) -> GND
- R27 pad 1: +5V -> Net-(U16A-~{WE})
- R27 pad 2: ~{REGEN_CS} -> +5V
- R28 pad 1: FONTSEL -> Net-(U17A-~{OE})
- R28 pad 2: GND -> +5V
- R29 pad 1: Net-(U24A-~{IACK}) -> A15
- R29 pad 2: +5V -> Net-(U20A-A14)
- R3 pad 2: Net-(U5-~{STATUS}) -> Net-(U27-CONF_DONE)
- R30 pad 1: Net-(U24A-~{CS}) -> GND
- R30 pad 2: +5V -> Net-(U20A-A14)
- R31 pad 1: Net-(U24A-~{DTACK}) -> A14
- R31 pad 2: +5V -> Net-(U20A-A13)
- R32 pad 1: Net-(U24A-~{INT}) -> GND
- R32 pad 2: +5V -> Net-(U20A-A13)
- R33 pad 1: I2C_SDA -> +5V
- R33 pad 2: +5V -> Net-(U20A-~{CE})
- R34 pad 1: I2C_SCL -> +5V
- R34 pad 2: +5V -> Net-(U20A-~{BYTE})
- R35 pad 1: Net-(U24A-~{RESET}) -> +5V
- R35 pad 2: +5V -> Net-(U20A-~{RST})
- R36 pad 1: Net-(U7F-VID_ACT) -> +5V
- R36 pad 2: Net-(D8-A) -> Net-(U20A-RY/~{BY})
- R37 pad 1: +5V -> /RAMDAC/R
- R37 pad 2: Net-(U11A-RY/~{BY}) -> GND
- R38 pad 1: +5V -> /RAMDAC/G
- R38 pad 2: Net-(U11A-A17) -> GND
- R39 pad 1: GND -> /RAMDAC/B
- R39 pad 2: Net-(U11A-A17) -> GND
- R44 pad 1: Net-(U25A-~{RESET}) -> Net-(U5F-HSYNC)
- R44 pad 2: +5V -> VAA
- R45 pad 1: Net-(U25A-~{CS}) -> Net-(U5F-VSYNC)
- R45 pad 2: +5V -> VAA
- R46 pad 1: +5V -> Net-(U5F-HSYNC)
- R46 pad 2: Net-(U25A-T0) -> Net-(C57-Pad1)
- R47 pad 1: +5V -> Net-(U5F-VSYNC)
- R47 pad 2: Net-(U25A-P10) -> Net-(C58-Pad1)
- R48 pad 1: +5V -> Net-(D5-K)
- R48 pad 2: Net-(U25A-T1) -> GND
- R49 pad 1: +5V -> Net-(U21A-~{RESET})
- R49 pad 2: Net-(U25A-P11) -> +5V
- R5 pad 1: Net-(U5-LED_RUN) -> Net-(U5B-SDOUT)
- R5 pad 2: Net-(D2-A) -> Net-(D1-A)
- R50 pad 1: GND -> I2C_SDA
- R50 pad 2: +5VP -> +5V
- R51 pad 1: Net-(U7F-HSYNC) -> I2C_SCL
- R51 pad 2: Net-(C9-Pad1) -> +5V
- R52 pad 1: Net-(U7F-VSYNC) -> Net-(U21A-~{CS})
- R52 pad 2: Net-(C10-Pad1) -> +5V
- R53 pad 1: Net-(U7F-HSYNC) -> Net-(U21A-~{DTACK})
- R54 pad 1: Net-(U7F-VSYNC) -> Net-(U21A-~{INT})
- R6 pad 1: Net-(U5-LED_FAIL) -> ~{SYSRESET}
- R6 pad 2: Net-(D3-A) -> Net-(JP1-A)
- R8 pad 1: Net-(U7C-DTACK_DRV) -> Net-(U27-LED_FAIL)
- R8 pad 2: GND -> Net-(D3-A)
- R9 pad 1: Net-(U7C-BERR_DRV) -> ~{FPGA_RESET}
- R9 pad 2: GND -> +5V
- RN1 pad 1: unconnected-(RN1-Pad1) -> D7
- RN1 pad 10: D9 -> unconnected-(RN1-Pad10)
- RN1 pad 12: D10 -> D9
- RN1 pad 13: D12 -> D11
- RN1 pad 14: D14 -> D13
- RN1 pad 15: unconnected-(RN1-Pad15) -> D15
- RN1 pad 16: D0 -> unconnected-(RN1-Pad16)
- RN1 pad 2: D7 -> D5
- RN1 pad 3: D5 -> D3
- RN1 pad 4: D3 -> D1
- RN1 pad 5: D1 -> D0
- RN1 pad 7: D15 -> D14
- RN1 pad 8: D13 -> D12
- RN1 pad 9: D11 -> D10
- RN4 pad 1: ~{B0WRITE} -> GND
- RN4 pad 2: ~{B0UDS} -> GND
- RN4 pad 3: ~{B0LDS} -> GND
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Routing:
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- added copper zone on In1.Cu, net (none)
- added copper zone on In4.Cu, net (none)
- added copper zone on In3.Cu, net +5V
- added copper zone on In3.Cu, net +5VP
- added copper zone on In3.Cu, net /RAMDAC/IREF
- added copper zone on B.Cu, net /RAMDAC/SINK
- added copper zone on F.Cu, net /RAMDAC/SINK
- added copper zone on In4.Cu, net GND
- added copper zone on In3.Cu, net VAA
- removed copper zone on B.Cu, net (none)
- removed copper zone on F.Cu, net (none)
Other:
- copper layers 4 -> 6
- board text added: "1"
- board text added: "2"
- board text added: "25.175MHz"
- board text added: "28.322MHz"
- board text added: "3"
- board text added: "4"
- board text added: "5"
- board text added: "6"
- board text added: "FAIL"
- board text added: "FPGA CFG"
- board text added: "ICSP"
- board text added: "JLCJLCJLCJLC"
- board text added: "K"
- board text added: "LAYER 1"
- board text added: "LAYER 2"
- board text added: "LAYER 3"
- board text added: "LAYER 4"
- board text added: "LAYER 5"
- board text added: "LAYER 6"
- board text added: "M"
- board text added: "REG_BASE0"
- board text added: "REG_BASE1"
- board text added: "REG_PRIV"
- board text added: "ROM_BASE0"
- board text added: "ROM_BASE1"
- board text added: "ROM_EN"
- board text added: "RUN"
- board text added: "UART"
- board text added: "VIDEO/KEYBOARD/MOUSE CARD TOM STOREY JUL 2025 REV ${REVISION}"
- board text added: "VID_RUN"
- board text added: "~{SYSRESET} MCU AUTOLOAD INH"
- board text removed: "VGA COMPATIBLE VIDEO CARD TOM STOREY JUN 2025 REV ${REVISION}"
